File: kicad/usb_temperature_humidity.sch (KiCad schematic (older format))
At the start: 15 parts, among them SW1 SW_SPDT, SW2 SW_SPDT, U1 SeeeduinoXIAO, U2 SHT-31, U3 PinHeader_XIAO, U4 PinHeader_XIAO, U5 SHT-31

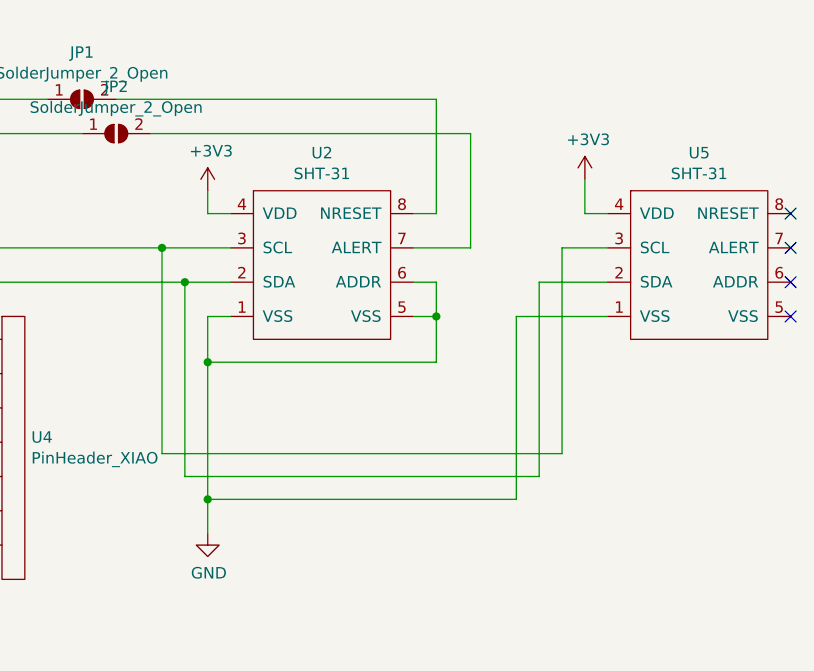
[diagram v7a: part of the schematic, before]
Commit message: シンボルをaliexpressのSHT-31に置き換えた
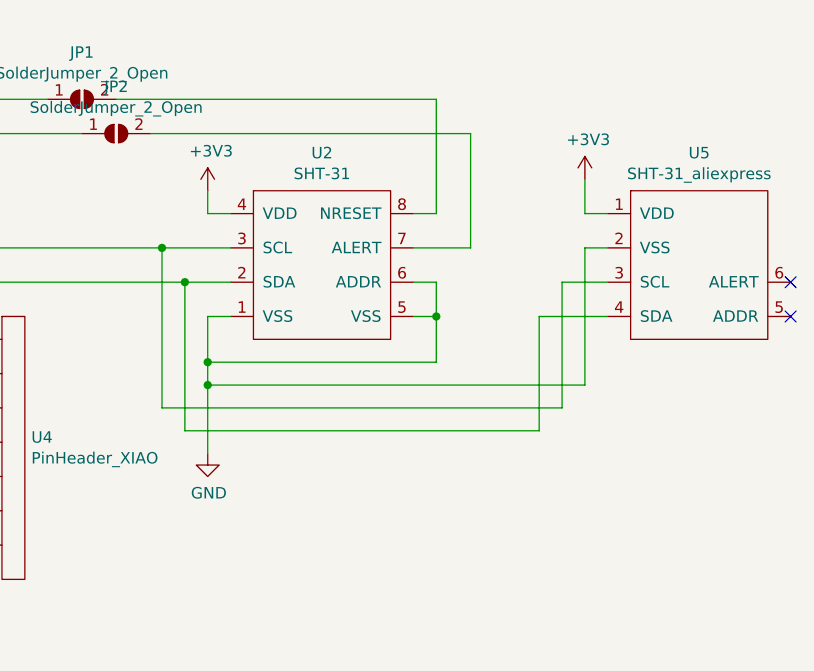
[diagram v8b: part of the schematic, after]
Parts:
- removed U5: SHT-31, kicad_mylib:SHT-31_aliexpress, symbol kicad_mylib:SHT-31
- added U5: SHT-31_aliexpress, kicad_mylib:SHT-31_aliexpress, symbol kicad_mylib:SHT-31_aliexpress
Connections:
- net +3V3: now also U5.1 (VDD)
- net GND: now also U5.2 (VSS)
- net at R3.2, U1.5 (PA8_A4_D4_SDA), U2.2 (SDA)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: now also U5.4 (SDA)
- net at R4.2, U1.6 (PA9_A5_D5_SCL), U2.3 (SCL)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: now also U5.3 (SCL)
- no-connect marks 12 -> 10
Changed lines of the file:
@@
 L power:GND #PWR08
 U 1 1 5F40CEFE
-P 5950 4450
-F 0 "#PWR08" H 5950 4200 50  0001 C CNN
-F 1 "GND" H 5955 4277 50  0000 C CNN
-F 2 "" H 5950 4450 50  0001 C CNN
-F 3 "" H 5950 4450 50  0001 C CNN
-	1    5950 4450
+P 5950 4100
+F 0 "#PWR08" H 5950 3850 50  0001 C CNN
+F 1 "GND" H 5955 3927 50  0000 C CNN
+F 2 "" H 5950 4100 50  0001 C CNN
+F 3 "" H 5950 4100 50  0001 C CNN
+	1    5950 4100
 	1    0    0    -1
 $EndComp
@@
 	1    0    0    -1
 $EndComp
-$Comp
-L kicad_mylib:SHT-31 U5
-U 1 1 5FDA7FE4
-P 7800 3600
-F 0 "U5" H 8100 4415 50  0000 C CNN
-F 1 "SHT-31" H 8100 4324 50  0000 C CNN
-F 2 "kicad_mylib:SHT-31_aliexpress" H 8350 4300 50  0001 C CNN
-F 3 "" H 8350 4300 50  0001 C CNN
-	1    7800 3600
-	1    0    0    -1
-$EndComp
-Connection ~ 5950 4300
-Wire Wire Line
-	5950 4300 5950 4450
-Wire Wire Line
-	7700 3500 7300 3500
-Wire Wire Line
-	7300 3500 7300 4300
-Wire Wire Line
-	7700 3200 7500 3200
-Wire Wire Line
-	7500 4100 5750 4100
-Wire Wire Line
-	5750 4100 5750 3200
-Wire Wire Line
-	7500 3200 7500 4100
+Wire Wire Line
+	5750 3900 5750 3200
 Connection ~ 5750 3200
 Wire Wire Line
 	5750 3200 4250 3200
 Wire Wire Line
-	7700 3350 7400 3350
-Wire Wire Line
-	7400 3350 7400 4200
-Wire Wire Line
-	7400 4200 5850 4200
-Wire Wire Line
-	5850 4200 5850 3350
+	5850 4000 5850 3350
 Connection ~ 5850 3350
 Wire Wire Line
@@
 Wire Wire Line
 	7600 3050 7700 3050
-NoConn ~ 8500 3500
-NoConn ~ 8500 3350
-NoConn ~ 8500 3200
-NoConn ~ 8500 3050
-Wire Wire Line
-	7300 4300 5950 4300
 Wire Wire Line
 	6950 3500 6950 3700
@@
 Connection ~ 6950 3500
 Connection ~ 5950 3700
-Wire Wire Line
-	5950 3700 5950 4300
+$Comp
+L kicad_mylib:SHT-31_aliexpress U5
+U 1 1 5FDDCCF5
+P 7800 3600
+F 0 "U5" H 8100 4415 50  0000 C CNN
+F 1 "SHT-31_aliexpress" H 8100 4324 50  0000 C CNN
+F 2 "kicad_mylib:SHT-31_aliexpress" H 8350 4300 50  0001 C CNN
+F 3 "" H 8350 4300 50  0001 C CNN
+	1    7800 3600
+	1    0    0    -1
+$EndComp
+Wire Wire Line
+	5950 3700 5950 3800
+Wire Wire Line
+	7600 3200 7700 3200
+Wire Wire Line
+	7600 3200 7600 3800
+Wire Wire Line
+	7600 3800 5950 3800
+Connection ~ 5950 3800
+Wire Wire Line
+	5950 3800 5950 4100
+Wire Wire Line
+	5850 4000 7400 4000
+Wire Wire Line
+	7400 4000 7400 3500
+Wire Wire Line
+	7400 3500 7700 3500
+Wire Wire Line
+	5750 3900 7500 3900
+Wire Wire Line
+	7500 3900 7500 3350
+Wire Wire Line
+	7500 3350 7700 3350
+NoConn ~ 8500 3500
+NoConn ~ 8500 3350
 $EndSCHEMATC
